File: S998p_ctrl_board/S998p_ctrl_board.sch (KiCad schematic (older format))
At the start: 29 parts, among them T1 BTA06-600C, U1 LM358

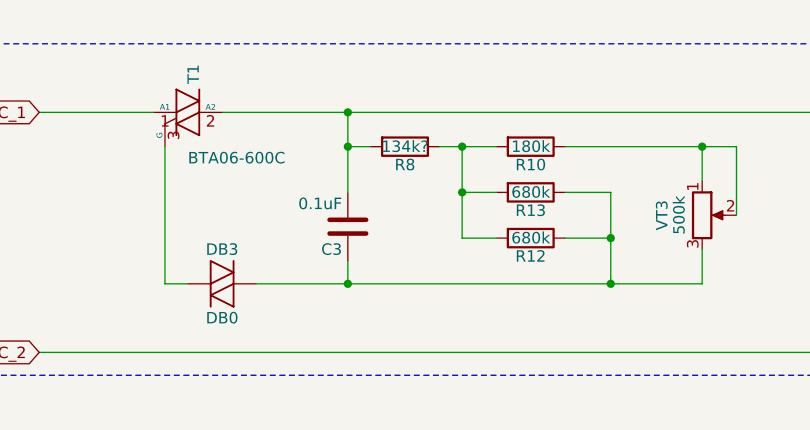
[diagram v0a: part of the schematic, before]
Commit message: R8 value fix. image fix.
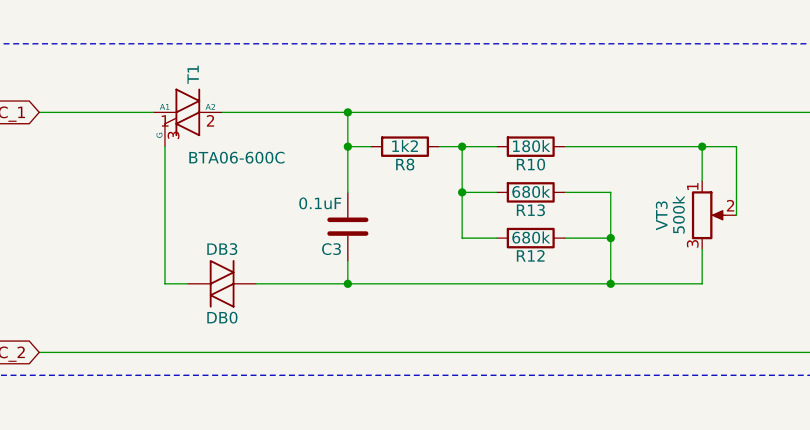
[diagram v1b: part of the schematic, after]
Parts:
- R8: value 134k? -> 1k2
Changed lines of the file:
@@
 P 2750 1550
 F 0 "R8" V 2830 1550 50  0000 C CNN
-F 1 "134k?" V 2750 1550 50  0000 C CNN
+F 1 "1k2" V 2750 1550 50  0000 C CNN
 F 2 "" V 2680 1550 50  0001 C CNN
 F 3 "~" H 2750 1550 50  0001 C CNN
